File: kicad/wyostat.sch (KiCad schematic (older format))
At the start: 86 parts, among them J1 24 V AC IN, J10 Y2, J11 G, J12 W1, J13 USB_microAB, J14 W2, J16 5V_SEL, J2 OUT1, J3 OUT2, J4 OUT3, J5 I2C_ext1, J6 RH, J7 RC, J8 C, J9 Y1, Q1 BTA204S, Q2 BTA204S, Q3 BTA204S, U1 MOC3063M, U2 MOC3063M, U3 MOC3063M, U4 Wemos-Lolin, U5 MAX17502FATB+T

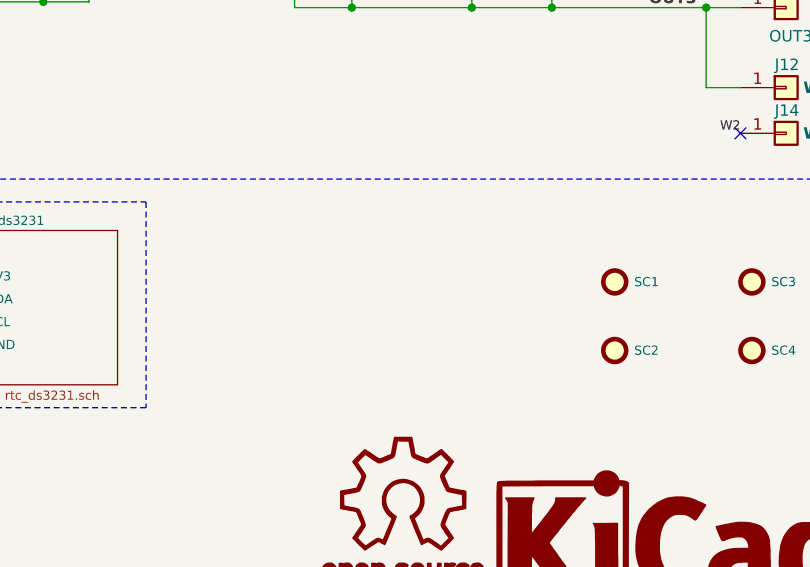
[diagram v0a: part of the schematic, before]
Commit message: increased clearances, added inverse text
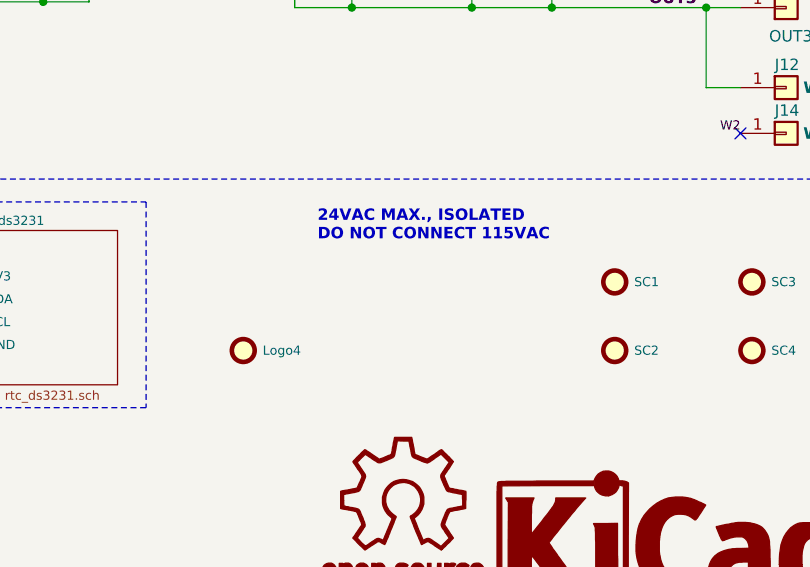
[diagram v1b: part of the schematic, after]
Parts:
- added Logo4: logo_snb, wyostat_fp:logo-skull_n_bones, symbol wyostat:SCREW
- Logo1: renamed from G1; footprint wyostat_fp:Logo-WL3 -> wyostat_fp:logo-WL3
- Logo2: renamed from G2; footprint wyostat_fp:OSHW_6mm -> wyostat_fp:logo-OSHW_6mm
- Logo3: renamed from G3; footprint wyostat_fp:KiCad-Logo2_6mm_SilkScreen -> wyostat_fp:logo-kicad_6mm_SilkScreen
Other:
- note added: "24VAC MAX., ISOLATED\nDO NOT CONNECT 115VAC"

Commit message: footprint corrections on PCB
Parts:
- removed C2, C4, C6: 47nF,63V, wyostat_fp:C_1210, symbol wyostat:C_NP
- removed R14, R2, R8: 0E, wyostat_fp:R_0805, symbol wyostat:R
- added Logo5: logo_warning, wyostat_fp:logo-warning, symbol wyostat:SCREW
- D5: footprint Diodes_SMD:D_SOD-323_HandSoldering -> wyostat_fp:D_SOD-323_HandSoldering
- JP1, JP2, JP3: footprint wyostat_fp:LED_0402 -> wyostat_fp:R_0805
- S1, S2, S3, S4: footprint wyostat_fp:SW_SPST_CK_KSCx -> wyostat_fp:SW_SPST_FSM6JSMA
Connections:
- net 24Vac-H: now also R1.1, R13.1, R7.1
- net 5V_IN1 renamed 5V_EXT
- net 5V_IN2 renamed 5V_USB
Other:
- note added: "BOM :\n1. ESP32 : Wemos Lolin\n2. Opto : MOC3063SR2M\n3. Triac : BTA204S-600E,118 (SMD)\n4. LED : LTST-C193KGKT-5A\n5. Bridge Rectifier : MDB6S\n6. PTC Fuse : 0ZCF0075AF2C\n7. DC-DC Converter : MAX17502\n8. 10nF/120V AC : LDEIB2100KA0N00\n9. 47nF/63V AC : LDEEB2470KA0N00\n10. Inductor L1 : ELL-8TP220MB\n11. 100uF/50V Elco : HHXC500ARA101MJA0G\n : EMZA630ADA101MJA0G"
- note added: "USB\n\nOFF\n\nEXT"
- note removed: "BOM :\n1. ESP32 : Wemos Lolin\n2. Opto : MOC3063SR2M\n3. Triac : BT134-600E,127 (TH)\n : BTA204S-600E,118 (SMD)\n4. LED : LTST-C193KGKT-5A\n5. Bridge Rectifier : MDB6S\n6. PTC Fuse : 0ZCF0075AF2C\n7. DC-DC Converter : MAX17502\n8. 10nF/120V AC : LDEIB2100KA0N00\n9. 47nF/63V AC : LDEEB2470KA0N00\n10. Inductor L1 : ELL-8TP220MB\n11. 100uF/50V Elco : HHXC500ARA101MJA0G\n : EMZA630ADA101MJA0G"
- moved on the sheet: Logo4

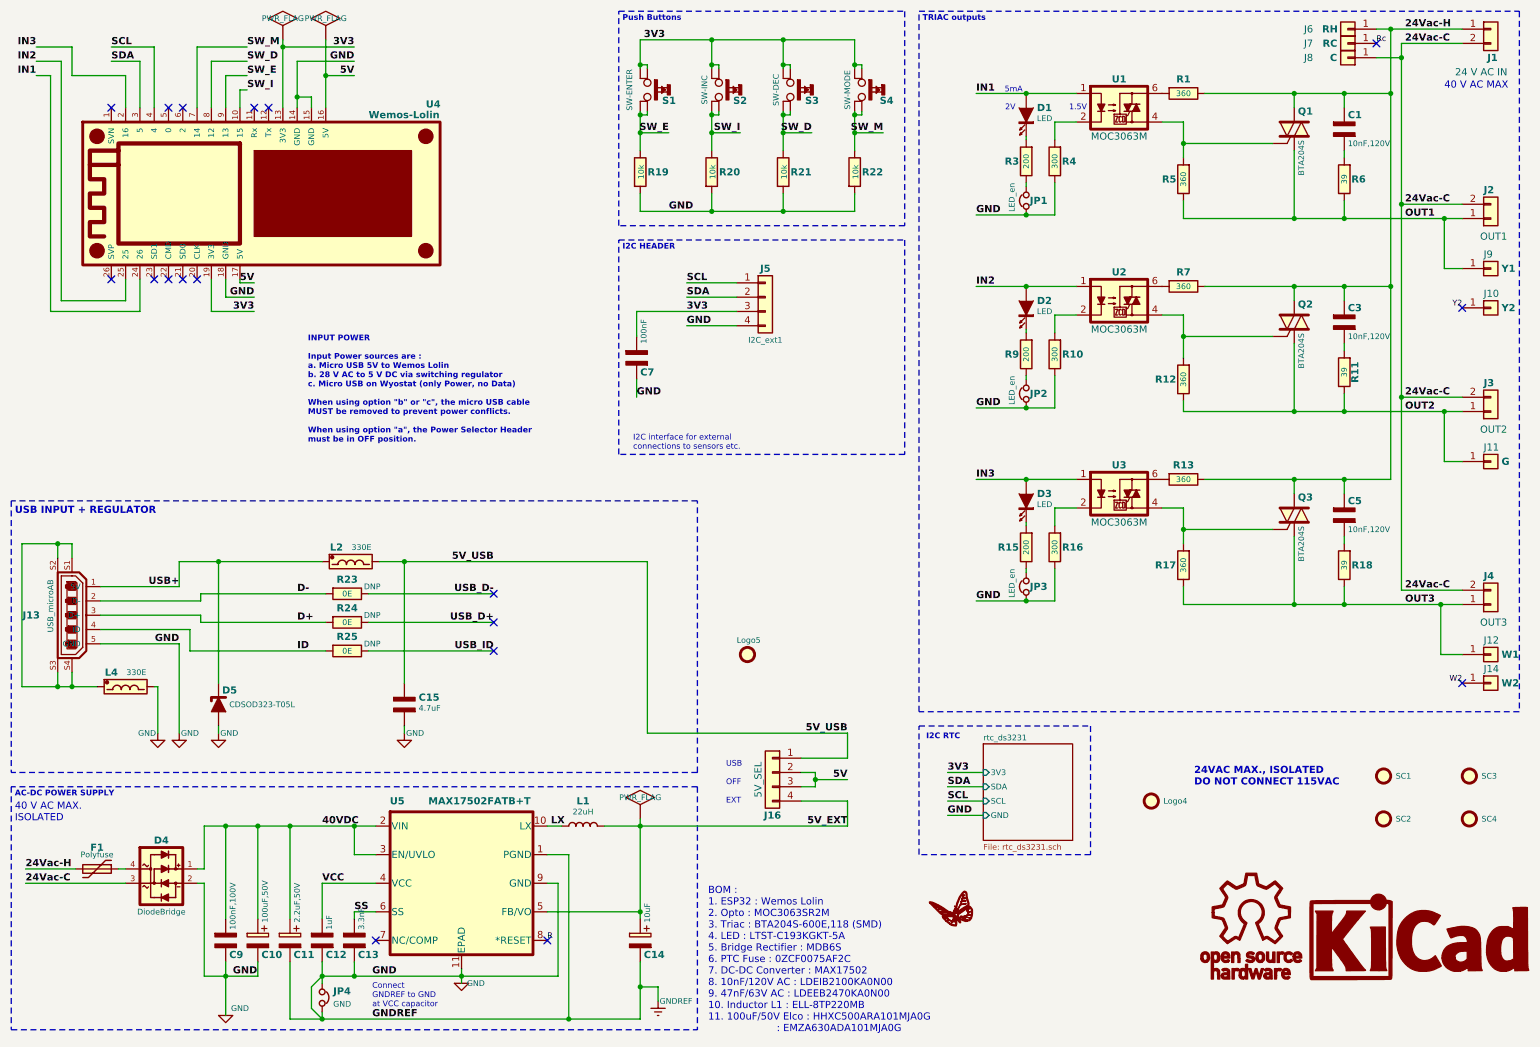
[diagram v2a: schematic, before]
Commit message: PCB updated for 2nd round of prototype
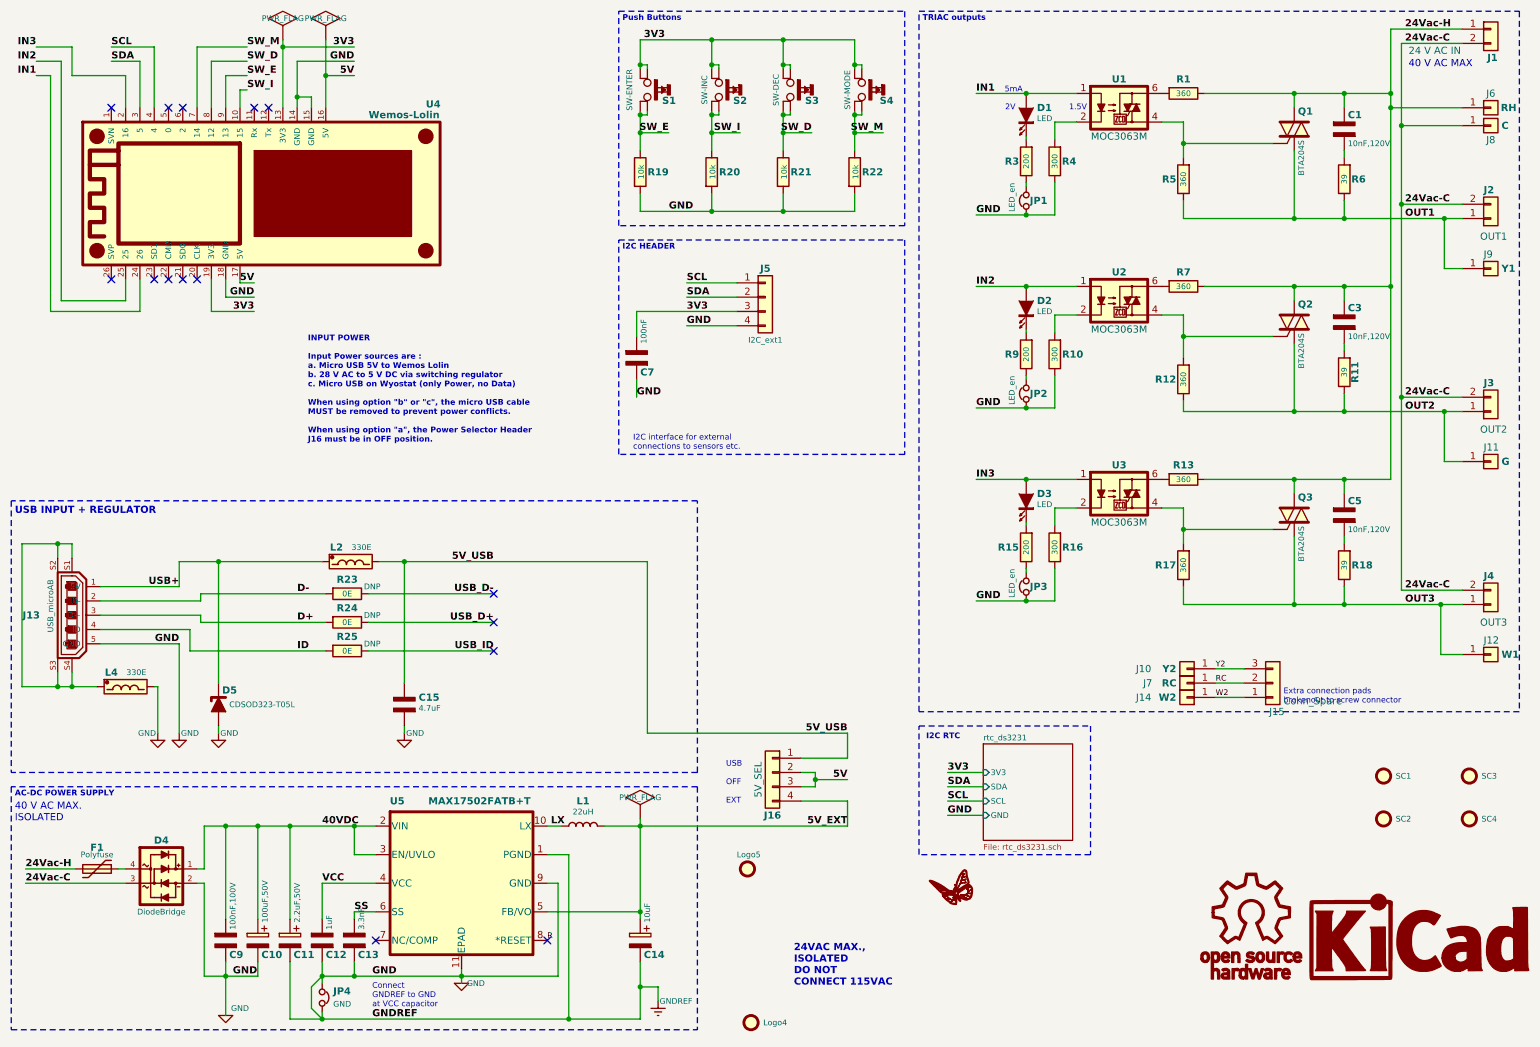
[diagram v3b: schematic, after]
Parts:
- added J15: Conn_Spare, wyostat_fp:TerminalBlock_Pheonix_MPT-2.54mm_3pol, symbol wyostat:Conn_01x03
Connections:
- net W2: now also J15.1 (Pin_1)
- net Y2: now also J15.3 (Pin_3)
- net Rc renamed RC
- net RC: now also J15.2 (Pin_2)
- no-connect marks 18 -> 15
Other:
- note added: "24VAC MAX.,\nISOLATED\nDO NOT \nCONNECT 115VAC"
- note added: "Extra connection pads\nbrokenout to screw connector"
- note added: "INPUT POWER\n\nInput Power sources are :\na. Micro USB 5V to Wemos Lolin\nb. 28 V AC to 5 V DC via switching regulator\nc. Micro USB on Wyostat (only Power, no Data)\n\nWhen using option "b" or "c", the micro USB cable\nMUST be removed to prevent power conflicts.\n\nWhen using option "a", the Power Selector Header\nJ16 must be in OFF position."
- note removed: "24VAC MAX., ISOLATED\nDO NOT CONNECT 115VAC"
- note removed: "BOM :\n1. ESP32 : Wemos Lolin\n2. Opto : MOC3063SR2M\n3. Triac : BTA204S-600E,118 (SMD)\n4. LED : LTST-C193KGKT-5A\n5. Bridge Rectifier : MDB6S\n6. PTC Fuse : 0ZCF0075AF2C\n7. DC-DC Converter : MAX17502\n8. 10nF/120V AC : LDEIB2100KA0N00\n9. 47nF/63V AC : LDEEB2470KA0N00\n10. Inductor L1 : ELL-8TP220MB\n11. 100uF/50V Elco : HHXC500ARA101MJA0G\n : EMZA630ADA101MJA0G"
- note removed: "INPUT POWER\n\nInput Power sources are :\na. Micro USB 5V to Wemos Lolin\nb. 28 V AC to 5 V DC via switching regulator\nc. Micro USB on Wyostat (only Power, no Data)\n\nWhen using option "b" or "c", the micro USB cable\nMUST be removed to prevent power conflicts.\n\nWhen using option "a", the Power Selector Header\nmust be in OFF position."
- moved on the sheet: J10, J14, J6, J7, J8, Logo4, Logo5
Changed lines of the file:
@@
 Sheet 1 2
 Title "WYOSTAT"
-Date "2018-03-12"
+Date "2018-04-05"
 Rev "rev 1"
 Comp "WyoLum"
-Comment1 ""
+Comment1 "https://github.com/wyolum/wyostat"
 Comment2 ""
 Comment3 ""
 Comment4 ""
 $EndDescr
-Text Notes 5450 7725 0    50   ~ 0
-BOM :\n1. ESP32 : Wemos Lolin\n2. Opto : MOC3063SR2M\n3. Triac : BTA204S-600E,118 (SMD)\n4. LED : LTST-C193KGKT-5A\n5. Bridge Rectifier : MDB6S\n6. PTC Fuse : 0ZCF0075AF2C\n7. DC-DC Converter : MAX17502\n8. 10nF/120V AC : LDEIB2100KA0N00\n9. 47nF/63V AC : LDEEB2470KA0N00\n10. Inductor L1 : ELL-8TP220MB\n11. 100uF/50V Elco : HHXC500ARA101MJA0G\n                      : EMZA630ADA101MJA0G
 $Comp
 L wyostat:MOC3063M U1
@@
 P 10925 700
 F 0 "J1" H 10900 500 50  0000 L CNB
-F 1 "24 V AC IN" H 10675 400 50  0000 L CNN
+F 1 "24 V AC IN" H 10350 550 50  0000 L CNN
 F 2 "wyostat_fp:TerminalBlock_Pheonix_MPT-2.54mm_2pol" H 10925 700 50  0001 C CNN
 F 3 "~" H 10925 700 50  0001 C CNN
@@
 Text Notes 600  6250 0    50   ~ 0
 40 V AC MAX.\nISOLATED
-Text Notes 10600 1125 0    50   ~ 0
+Text Notes 10350 975  0    50   ~ 0
 40 V AC MAX
 Wire Wire Line
@@
 	10725 700  10225 700
 Wire Wire Line
-	10300 800  10300 900
+	10300 800  10300 1375
 Wire Wire Line
 	10300 800  10725 800
@@
 Connection ~ 10225 1150
 Wire Wire Line
-	10225 700  10225 1150
-Wire Wire Line
 	9900 2500 10225 2500
 Connection ~ 9900 2500
 Connection ~ 10225 2500
 Wire Wire Line
-	10225 1150 10225 2500
+	10225 1150 10225 1250
 Wire Wire Line
 	10225 3850 9900 3850
@@
 	10225 2500 10225 3850
 Text Notes 2650 3600 0    40   ~ 8
-INPUT POWER\n\nInput Power sources are :\na. Micro USB 5V to Wemos Lolin\nb. 28 V AC to 5 V DC via switching regulator\nc. Micro USB on Wyostat (only Power, no Data)\n\nWhen using option "b" or "c", the micro USB cable\nMUST be removed to prevent power conflicts.\n\nWhen using option "a", the Power Selector Header\nmust be in OFF position.
+INPUT POWER\n\nInput Power sources are :\na. Micro USB 5V to Wemos Lolin\nb. 28 V AC to 5 V DC via switching regulator\nc. Micro USB on Wyostat (only Power, no Data)\n\nWhen using option "b" or "c", the micro USB cable\nMUST be removed to prevent power conflicts.\n\nWhen using option "a", the Power Selector Header\nJ16 must be in OFF position.
 Text Label 2750 6675 0    50   ~ 10
 VCC
@@
 L wyostat:LOGO_WL Logo1
 U 1 1 5AC0C12D
-P 7175 6875
-F 0 "Logo1" H 7175 6739 60  0001 C CNN
-F 1 "LOGO_WL" H 7175 7011 60  0001 C CNN
-F 2 "wyostat_fp:logo-WL3" H 7175 6875 60  0001 C CNN
-F 3 "" H 7175 6875 60  0001 C CNN
-F 4 "Value" H 7175 6875 50  0001 C CNN "manf#"
-	1    7175 6875
+P 7175 6725
+F 0 "Logo1" H 7175 6589 60  0001 C CNN
+F 1 "LOGO_WL" H 7175 6861 60  0001 C CNN
+F 2 "wyostat_fp:logo-WL3" H 7175 6725 60  0001 C CNN
+F 3 "" H 7175 6725 60  0001 C CNN
+F 4 "Value" H 7175 6725 50  0001 C CNN "manf#"
+	1    7175 6725
 	1    0    0    -1
 $EndComp
@@
 L wyostat:Conn_01x01 J6
 U 1 1 5AB1854D
-P 9925 700
-F 0 "J6" H 10200 700 50  0000 C CNN
-F 1 "RH" H 10050 700 50  0000 C CNB
-F 2 "wyostat_fp:pad_rect_smd" H 9925 700 50  0001 C CNN
-F 3 "" H 9925 700 50  0001 C CNN
-	1    9925 700
-	-1   0    0    1
+P 10925 1250
+F 0 "J6" H 10925 1350 50  0000 C CNN
+F 1 "RH" H 11050 1250 50  0000 C CNB
+F 2 "wyostat_fp:pad_rect_smd" H 10925 1250 50  0001 C CNN
+F 3 "" H 10925 1250 50  0001 C CNN
+	1    10925 1250
+	1    0    0    -1
 $EndComp
 $Comp
 L wyostat:Conn_01x01 J7
 U 1 1 5AB186B9
-P 9925 800
-F 0 "J7" H 10200 800 50  0000 C CNN
-F 1 "RC" H 10050 800 50  0000 C CNB
-F 2 "wyostat_fp:pad_rect_smd" H 9925 800 50  0001 C CNN
-F 3 "" H 9925 800 50  0001 C CNN
-	1    9925 800
+P 8800 5275
+F 0 "J7" H 9075 5275 50  0000 C CNN
+F 1 "RC" H 8925 5275 50  0000 C CNB
+F 2 "wyostat_fp:pad_rect_smd" H 8800 5275 50  0001 C CNN
+F 3 "" H 8800 5275 50  0001 C CNN
+	1    8800 5275
 	-1   0    0    1
 $EndComp
@@
 L wyostat:Conn_01x01 J8
 U 1 1 5AB18767
-P 9925 900
-F 0 "J8" H 10200 900 50  0000 C CNN
-F 1 "C" H 10025 900 50  0000 C CNB
-F 2 "wyostat_fp:pad_rect_smd" H 9925 900 50  0001 C CNN
-F 3 "" H 9925 900 50  0001 C CNN
-	1    9925 900
-	-1   0    0    1
+P 10925 1375
+F 0 "J8" H 10925 1275 50  0000 C CNN
+F 1 "C" H 11025 1375 50  0000 C CNB
+F 2 "wyostat_fp:pad_rect_smd" H 10925 1375 50  0001 C CNN
+F 3 "" H 10925 1375 50  0001 C CNN
+	1    10925 1375
+	1    0    0    -1
 $EndComp
 Wire Wire Line
-	10225 700  10125 700
-Connection ~ 10225 700
-Wire Wire Line
-	10125 900  10300 900
-Connection ~ 10300 900
+	10725 1375 10300 1375
+Connection ~ 10300 1375
 Wire Wire Line
-	10300 900  10300 1925
-NoConn ~ 10125 800
+	10300 1375 10300 1925
 $Comp
 L wyostat:Conn_01x01 J11
@@
 L wyostat:Conn_01x01 J10
 U 1 1 5ABA96DB
-P 10925 2650
-F 0 "J10" H 10875 2750 50  0000 L CNN
-F 1 "Y2" H 11000 2650 50  0000 L CNB
-F 2 "wyostat_fp:pad_rect_smd" H 10925 2650 50  0001 C CNN
-F 3 "" H 10925 2650 50  0001 C CNN
-	1    10925 2650
-	1    0    0    -1
+P 8800 5175
+F 0 "J10" H 9050 5175 50  0000 L CNN
+F 1 "Y2" H 8875 5175 50  0000 L CNB
+F 2 "wyostat_fp:pad_rect_smd" H 8800 5175 50  0001 C CNN
+F 3 "" H 8800 5175 50  0001 C CNN
+	1    8800 5175
+	-1   0    0    1
 $EndComp
-NoConn ~ 10725 2650
 Wire Wire Line
 	10725 2375 10600 2375
@@
 L wyostat:Conn_01x01 J14
 U 1 1 5AD0E58F
-P 10925 5275
-F 0 "J14" H 10875 5375 50  0000 L CNN
-F 1 "W2" H 11000 5275 50  0000 L CNB
-F 2 "wyostat_fp:pad_rect_smd" H 10925 5275 50  0001 C CNN
-F 3 "" H 10925 5275 50  0001 C CNN
-	1    10925 5275
-	1    0    0    -1
+P 8800 5375
+F 0 "J14" H 9050 5375 50  0000 L CNN
+F 1 "W2" H 8875 5375 50  0000 L CNB
+F 2 "wyostat_fp:pad_rect_smd" H 8800 5375 50  0001 C CNN
+F 3 "" H 8800 5375 50  0001 C CNN
+	1    8800 5375
+	-1   0    0    1
 $EndComp
-NoConn ~ 10725 5275
 Wire Wire Line
 	10725 5075 10575 5075
@@
 Wire Wire Line
 	10575 4725 10725 4725
-Text Label 10725 2650 2    40   ~ 0
+Text Label 9000 5175 0    40   ~ 0
 Y2
-Text Label 10725 5275 2    40   ~ 0
+Text Label 9000 5375 0    40   ~ 0
 W2
-Text Label 10125 800  0    40   ~ 0
-Rc
 $Bitmap
-Pos 8550 5875
+Pos 5750 7350
 Scale 1.000000
 Data
@@
 L wyostat:SCREW Logo4
 U 1 1 5AB3F94C
-P 8550 6100
-F 0 "Logo4" H 8635 6100 40  0000 L CNN
-F 1 "logo_snb" H 8550 6200 40  0001 C CNN
-F 2 "wyostat_fp:logo-skull_n_bones" H 8550 6100 60  0001 C CNN
-F 3 "" H 8550 6100 60  0000 C CNN
-F 4 "Value" H 8550 6100 50  0001 C CNN "manf#"
-	1    8550 6100
+P 5750 7650
+F 0 "Logo4" H 5835 7650 40  0000 L CNN
+F 1 "logo_snb" H 5750 7750 40  0001 C CNN
+F 2 "wyostat_fp:logo-skull_n_bones" H 5750 7650 60  0001 C CNN
+F 3 "" H 5750 7650 60  0000 C CNN
+F 4 "Value" H 5750 7650 50  0001 C CNN "manf#"
+	1    5750 7650
 	1    0    0    -1
 $EndComp
-Text Notes 8850 6000 0    50   ~ 10
-24VAC MAX., ISOLATED\nDO NOT CONNECT 115VAC
+Text Notes 6050 7400 0    50   ~ 10
+24VAC MAX.,\nISOLATED\nDO NOT \nCONNECT 115VAC
 Wire Wire Line
 	8775 2025 9550 2025
@@
 	8775 2700 8625 2700
 $Bitmap
-Pos 5725 5325
+Pos 5725 6850
 Scale 1.000000
 Data
@@
 L wyostat:SCREW Logo5
 U 1 1 5AE0052A
-P 5725 5075
-F 0 "Logo5" H 5650 5175 40  0000 L CNN
-F 1 "logo_warning" H 5725 5175 40  0001 C CNN
-F 2 "wyostat_fp:logo-warning" H 5725 5075 60  0001 C CNN
-F 3 "" H 5725 5075 60  0000 C CNN
-F 4 "Value" H 5725 5075 50  0001 C CNN "manf#"
-	1    5725 5075
+P 5725 6575
+F 0 "Logo5" H 5650 6675 40  0000 L CNN
+F 1 "logo_warning" H 5725 6675 40  0001 C CNN
+F 2 "wyostat_fp:logo-warning" H 5725 6575 60  0001 C CNN
+F 3 "" H 5725 6575 60  0000 C CNN
+F 4 "Value" H 5725 6575 50  0001 C CNN "manf#"
+	1    5725 6575
 	1    0    0    -1
 $EndComp
@@
 Text Notes 5575 6125 0    40   ~ 0
 USB\n\nOFF\n\nEXT
+Wire Wire Line
+	10225 700  10225 1150
+Wire Wire Line
+	10725 1250 10225 1250
+Connection ~ 10225 1250
+Wire Wire Line
+	10225 1250 10225 2500
+Text Label 9000 5275 0    40   ~ 0
+RC
+$Comp
+L wyostat:Conn_01x03 J15
+U 1 1 5AD6DCBB
+P 9400 5275
+F 0 "J15" H 9375 5475 50  0000 L CNN
+F 1 "Conn_Spare" H 9475 5400 50  0000 L CNN
+F 2 "wyostat_fp:TerminalBlock_Pheonix_MPT-2.54mm_3pol" H 9400 5275 50  0001 C CNN
+F 3 "" H 9400 5275 50  0001 C CNN
+	1    9400 5275
+	1    0    0    1
+$EndComp
+Wire Wire Line
+	9000 5175 9200 5175
+Wire Wire Line
+	9000 5275 9200 5275
+Wire Wire Line
+	9000 5375 9200 5375
+Text Notes 9475 5425 0    40   ~ 0
+Extra connection pads\nbrokenout to screw connector
 $EndSCHEMATC
